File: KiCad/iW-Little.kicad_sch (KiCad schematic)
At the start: 27 parts, among them J1 USB_C_Receptacle_USB2.0, J3 Conn_01x10, J4 Conn_01x08, J5 Conn_02x02_Odd_Even, SW1 SW_Push, SW2 SW_Push, U1 STM32F030F4Px, U2 CH343P, U3 USBLC6-2P6, U4 AP2112K-3.3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

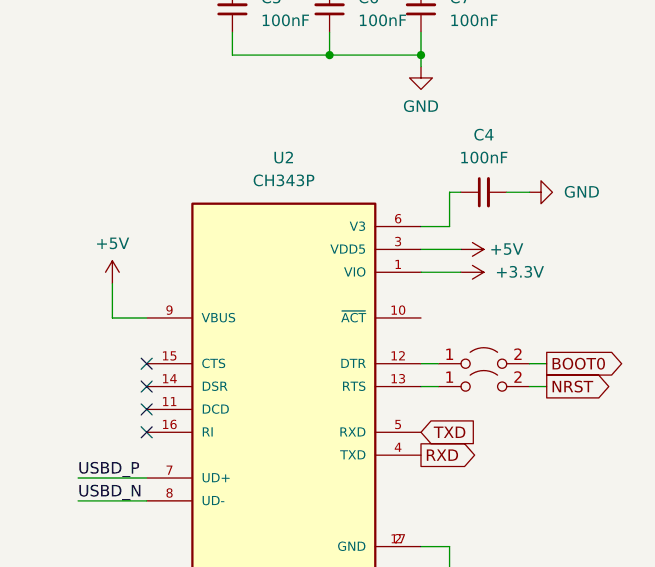
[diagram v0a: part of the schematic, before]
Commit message: size changed
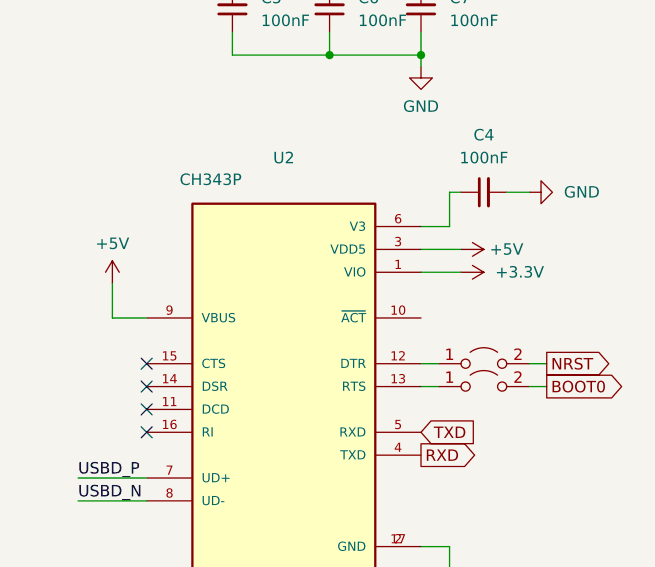
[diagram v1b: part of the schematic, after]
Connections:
- net BOOT0: now also JP2.2 (B); no longer JP1.2 (B)
- net NRST: now also JP1.2 (B); no longer JP2.2 (B)
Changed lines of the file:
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@@
 	(global_label "NRST"
 		(shape output)
-		(at 270.51 74.295 0)
+		(at 270.51 71.755 0)
 		(fields_autoplaced yes)
 		(effects
@@
 		)
 		(property "Intersheetrefs" "${INTERSHEET_REFS}"
-			(at 278.2728 74.295 0)
+			(at 278.2728 71.755 0)
 			(effects
 				(font
@@
 	(global_label "BOOT0"
 		(shape output)
-		(at 270.51 71.755 0)
+		(at 270.51 74.295 0)
 		(fields_autoplaced yes)
 		(effects
@@
 		)
 		(property "Intersheetrefs" "${INTERSHEET_REFS}"
-			(at 279.6033 71.755 0)
+			(at 279.6033 74.295 0)
 			(effects
 				(font
@@
 		(on_board yes)
 		(dnp no)
-		(fields_autoplaced yes)
 		(property "Reference" "U2"
 			(at 241.3 48.895 0)
@@
 		)
 		(property "Value" "CH343P"
-			(at 241.3 51.435 0)
-			(effects
-				(font
+			(at 233.172 51.308 0)
+			(effects
+				(font
